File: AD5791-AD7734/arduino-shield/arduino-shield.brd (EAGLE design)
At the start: 102 x 53.8 mm, 27 parts, among them IC1 74ABT125PW, IC2 74ABT125PW, X1 22-23-2021, X2 22-23-2021, X3 22-23-2021, X4 22-23-2021, X5 22-23-2021

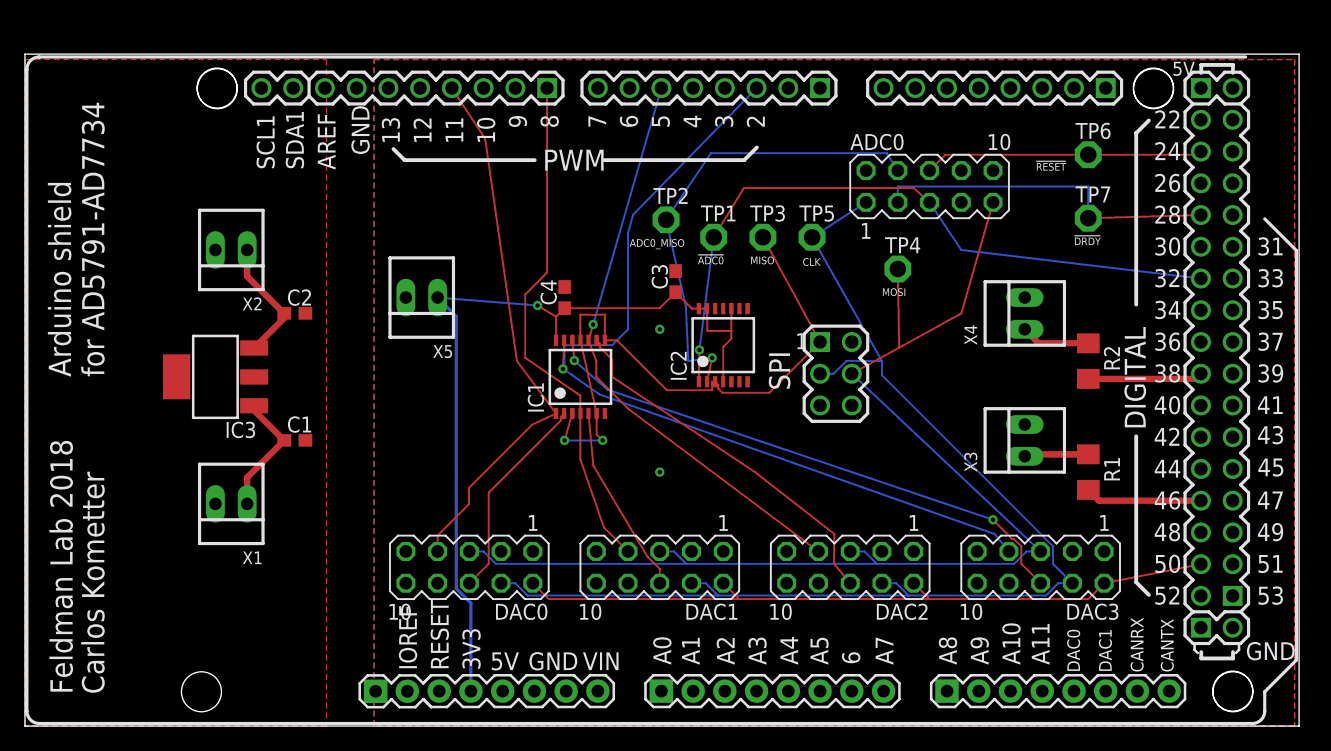
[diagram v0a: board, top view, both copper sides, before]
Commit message: Part numbers renumbered.
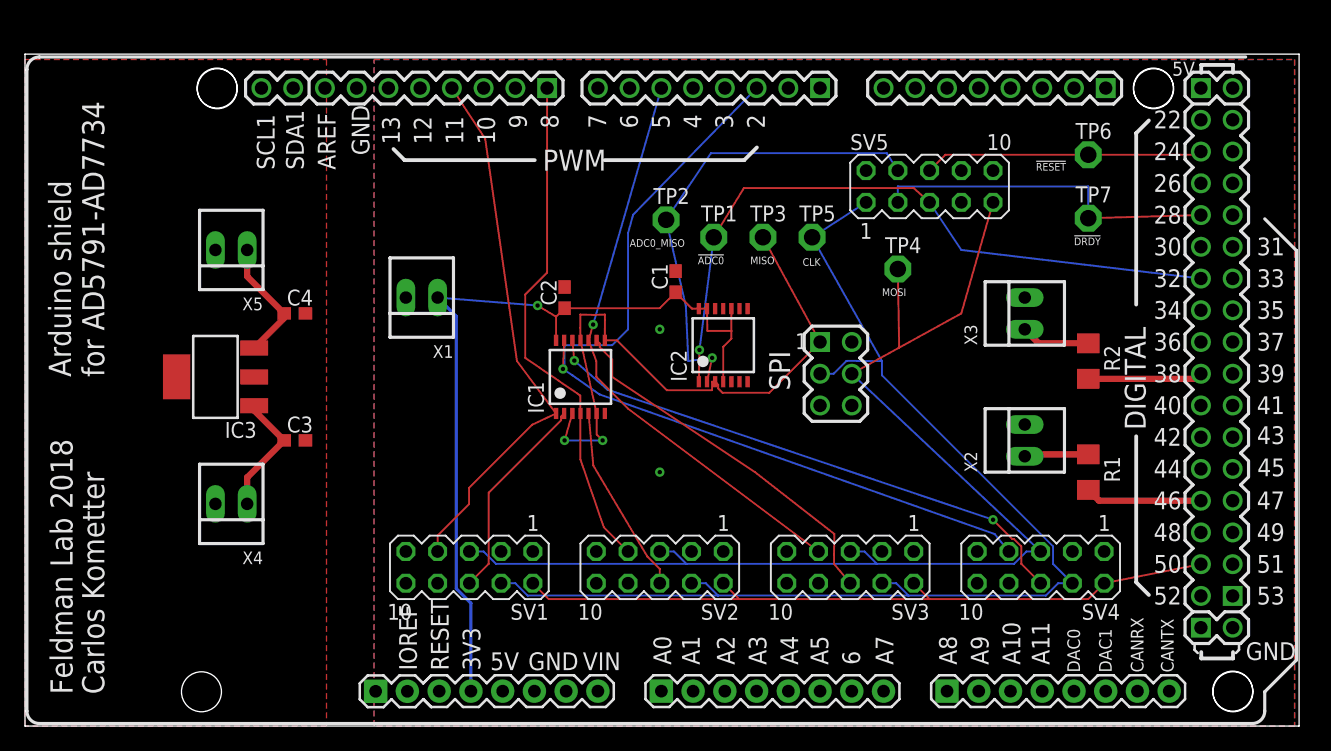
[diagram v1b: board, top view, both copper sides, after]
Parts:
- C1: value 1uF -> 0.1uF
- C2: value 1.5uF -> 0.1uF
- C3: value 0.1uF -> 1uF
- C4: value 0.1uF -> 1.5uF
- R1, R2: value 300 mR -> 330 mR
- moved X2 65.3 mm to (80.0, 22.9), turned to 90 degrees
- moved X4 65.3 mm to (16.5, 17.8), turned to 180 degrees
- moved C1 33.0 mm to (52.1, 35.6), turned to 90 degrees
- moved C3 33.0 mm to (21.6, 22.9), turned to 0 degrees
- moved X1 22.5 mm to (31.8, 34.3)
- moved C2 21.6 mm to (43.2, 34.3), turned to 90 degrees
- moved C4 21.6 mm to (21.6, 33.0), turned to 0 degrees
- moved X5 15.7 mm to (16.5, 38.1)
- moved X3 10.2 mm to (80.0, 33.0)
- renumbered ADC0 to SV5, DAC0 to SV1, DAC1 to SV2, DAC2 to SV3, DAC3 to SV4
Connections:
- net AGND: now also C3.2, C4.2, X4.2, X5.2; no longer C1.2, C2.2, X1.2, X2.2
- net GND: now also C1.2, C2.2, X1.2, X2.2; no longer C3.2, C4.2, X4.2, X5.2
- net N$1: now also C3.1, X4.1; no longer C1.1, X1.1
- net N$2: now also C4.1, X5.1; no longer C2.1, X2.1
- net N$4: now also X2.1; no longer X3.1
- net N$7: now also X3.1; no longer X4.1
- net VCC: now also C1.1, C2.1, X1.1; no longer C3.1, C4.1, X5.1
